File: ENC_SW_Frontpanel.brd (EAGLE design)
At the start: 39.4 x 38.1 mm, 11 parts, among them SW1 SPDT

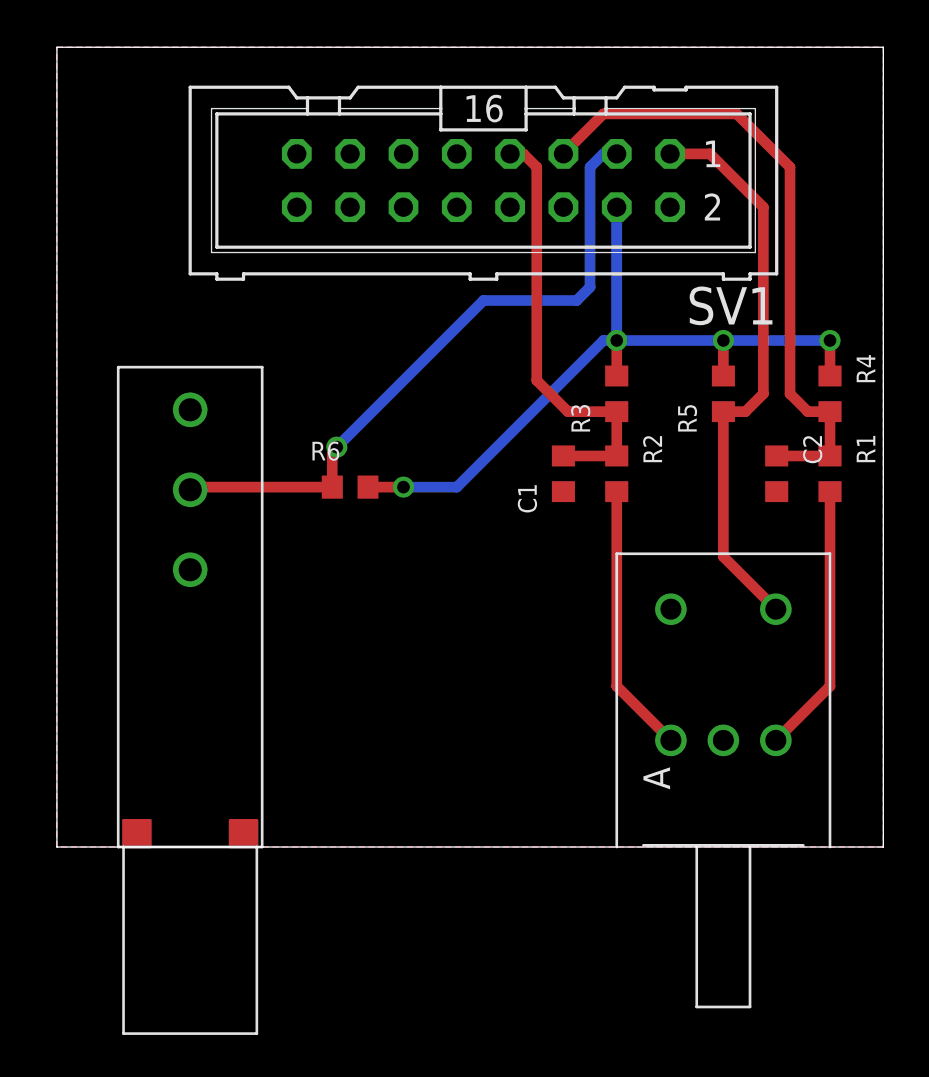
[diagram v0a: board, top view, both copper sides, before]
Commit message: Re-routed several mcu-accessory boards to be (mostly) single-layer
Will make printing easier on LKPF machine.
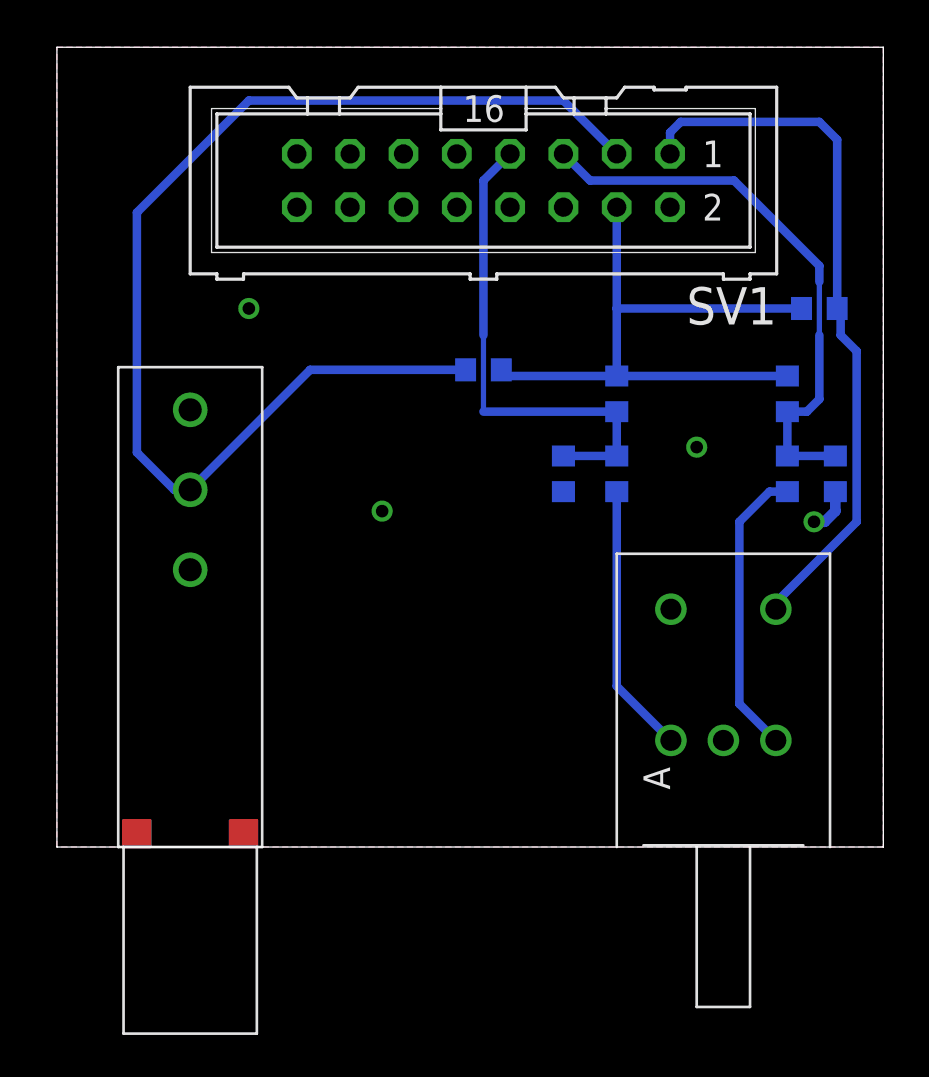
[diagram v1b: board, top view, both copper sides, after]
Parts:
- moved R6 8.46 mm to (14.0, 22.7), flipped to the bottom, turned to 180 degrees
- moved R5 6.12 mm to (30.0, 25.7), flipped to the bottom, turned to 0 degrees
- moved C2 2.79 mm to (30.7, 17.8), flipped to the bottom
- moved R1 2.03 mm to (28.4, 17.8), flipped to the bottom
- moved R4 2.03 mm to (28.4, 21.6), flipped to the bottom
- flipped C1 to the bottom
- flipped R2 to the bottom
- flipped R3 to the bottom
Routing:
- net SW1: track 31.3 -> 56.3 mm, vias 1 -> 0
- net ENC_SW: track 27.1 -> 33.9 mm
- net VDD: track 36.3 -> 30.8 mm, vias 4 -> 0
- net ENC_B: track 30.3 -> 26.9 mm
- net ENC_A: track 20.8 -> 23.8 mm
- net GND: track 0.00 -> 2.15 mm, vias 0 -> 4
- net N$4: track 12.9 -> 14.0 mm

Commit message: Enlarged holes for switch; redid SW-ENC-Frontpanel
Now switch and rotary encoder are 0.75" separated.
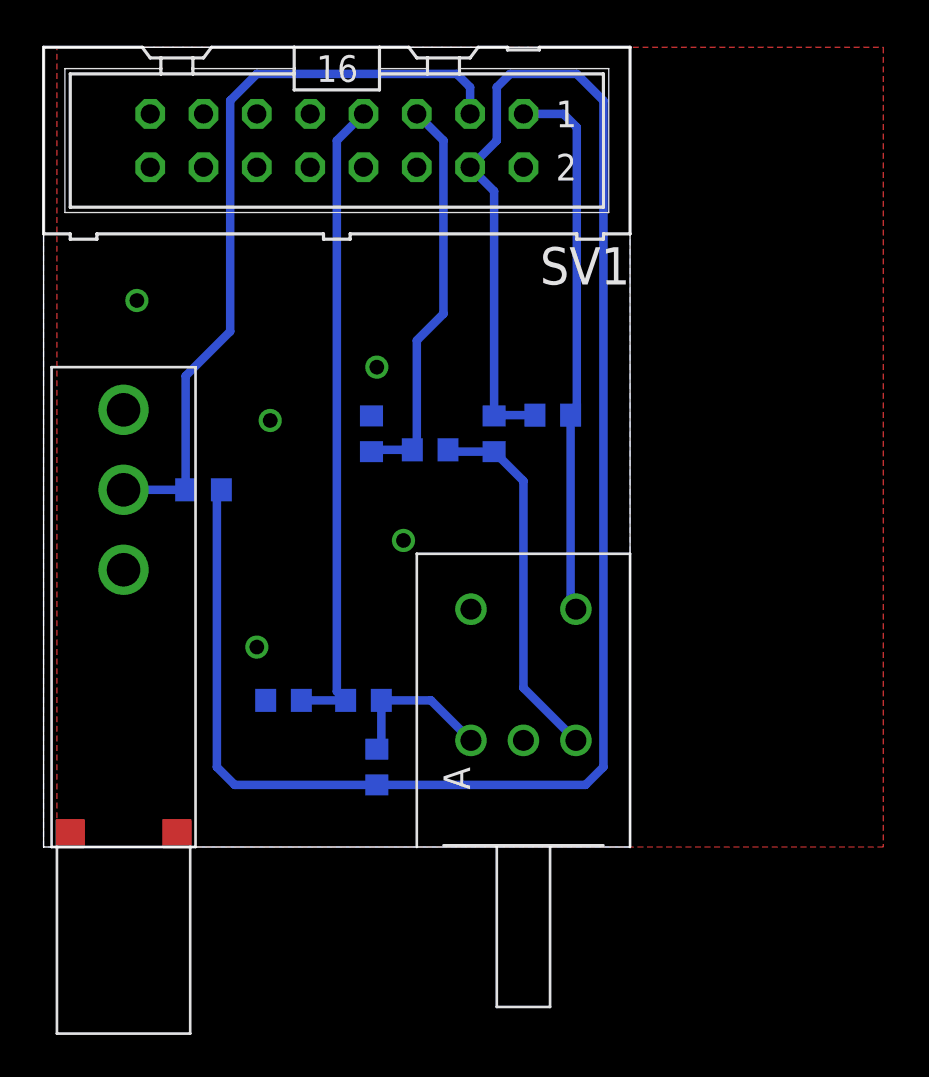
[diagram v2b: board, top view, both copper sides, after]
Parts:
- moved C2 22.2 mm to (8.64, 19.7), turned to 90 degrees
- moved R3 21.1 mm to (8.89, 3.81), turned to 270 degrees
- moved C1 17.2 mm to (4.45, 6.99), turned to 180 degrees
- moved R1 17.1 mm to (11.4, 18.9), turned to 180 degrees
- moved R2 16.2 mm to (8.26, 6.99), turned to 180 degrees
- moved R6 14.5 mm to (0.64, 17.0)
- moved R4 14.1 mm to (14.5, 19.7)
- moved R5 13.7 mm to (17.3, 20.6)
- moved ENC1 9.52 mm to (15.9, 5.08)
- moved SV1 7.24 mm to (6.99, 33.7)
- moved SW1 3.17 mm to (-3.17, 0.00)
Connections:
- net ENC_A: no longer R3.1
- net ENC_B: no longer R4.2
- net GND: now also SW1.IN2; no longer SW1.P$5
- net N$4: now also R4.2
- net N$5: now also R3.1
- net SW1: now also SW1.OUT; no longer SW1.P$4
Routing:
- net VDD: track 30.8 -> 88.7 mm
- net SW1: track 56.3 -> 35.9 mm
- net ENC_SW: track 33.9 -> 26.0 mm
- net ENC_B: track 26.9 -> 19.1 mm
- net ENC_A: track 23.8 -> 30.8 mm
- net N$5: track 12.9 -> 7.47 mm
- net N$4: track 14.0 -> 17.6 mm
- net GND: track 2.15 -> 0.00 mm, vias 4 -> 5
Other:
- board size 39.4 x 38.1 mm -> 27.9 x 38.1 mm
